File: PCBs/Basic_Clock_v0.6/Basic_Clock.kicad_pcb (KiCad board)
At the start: 2 copper layers, 97.8 x 71.1 mm, 37 parts, among them J1 Conn_01x04_Female, J3 Screw_Terminal_01x02, J4 Screw_Terminal_01x02, J5 Conn_01x03_Female, SW2 SW_Push, SW3 SW_Push, SW4 SW_Push, U1 LM317_TO-220, U2 ATmega328P-PU, U3 MAX485E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

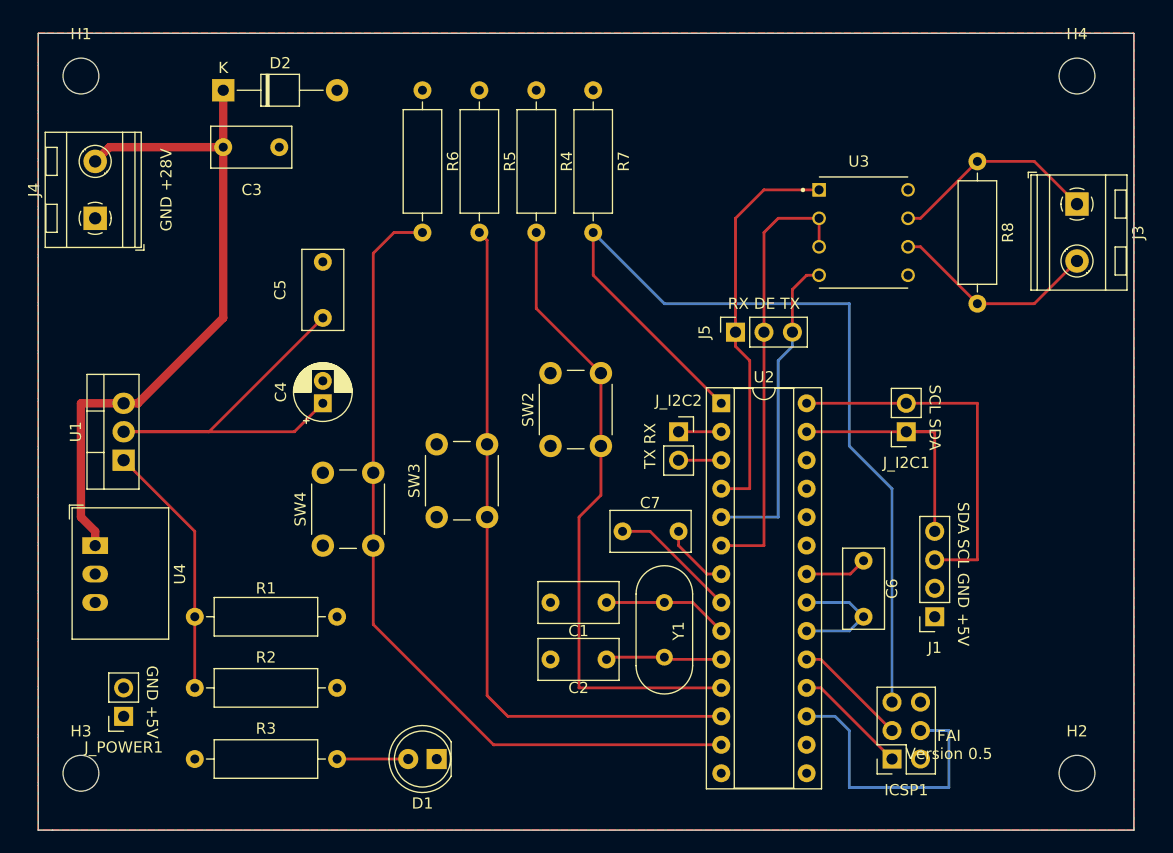
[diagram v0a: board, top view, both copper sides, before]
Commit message: Fixed ICSP Pinout
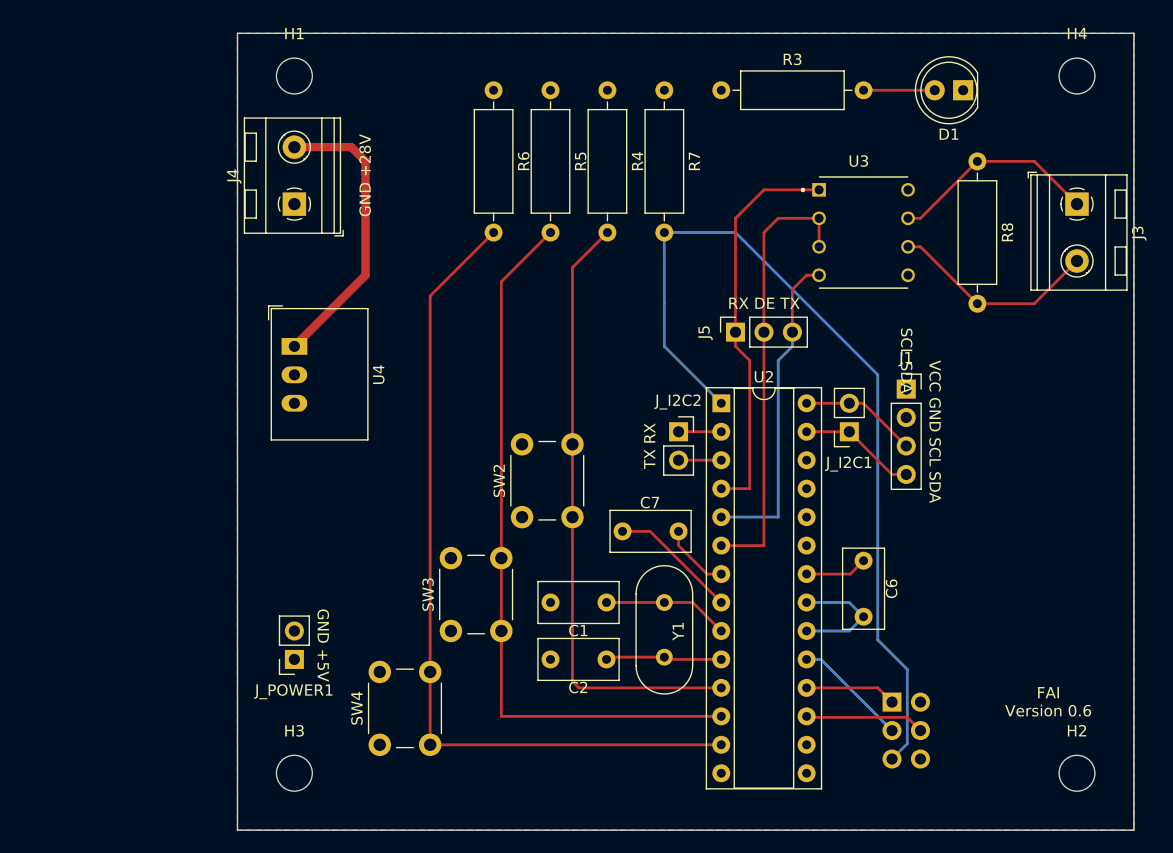
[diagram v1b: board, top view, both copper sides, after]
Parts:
- removed C3, C5: 100nF, Capacitor_THT:C_Rect_L7.0mm_W3.5mm_P5.00mm
- removed C4: 1uF, Capacitor THT:CP_Radial_D5.0mm_P2.00mm
- removed D2: D, Diode THT:D_T-1_P10.16mm_Horizontal
- removed R1: 240, Resistor:R_Axial_DIN0309_L9.0mm_D3.2mm_P12.70mm_Horizontal
- removed R2: 720, Resistor:R_Axial_DIN0309_L9.0mm_D3.2mm_P12.70mm_Horizontal
- removed U1: LM317_TO-220, TO SOT THT:TO-220-3_Vertical
- ICSP1: moved to B.Cu
- moved R3 76.0 mm to (97.8, 109.2)
- moved D1 76.0 mm to (119.4, 109.2)
- moved U4 25.1 mm to (59.7, 132.1)
- moved J1 20.5 mm to (114.3, 135.9), turned to 0 degrees
- moved H1 19.0 mm to (59.7, 108.0)
- moved H3 19.0 mm to (59.7, 170.2)
- moved SW4 18.5 mm to (67.3, 167.6)
- moved J4 17.8 mm to (59.7, 119.4)
- moved J_POWER1 16.1 mm to (59.7, 160.0)
- moved SW3 10.2 mm to (73.7, 157.5)
- moved SW2 6.84 mm to (80.0, 147.3)
- moved R4 6.35 mm to (87.6, 109.2)
- moved R5 6.35 mm to (82.5, 109.2)
- moved R6 6.35 mm to (77.5, 109.2)
- moved R7 6.35 mm to (92.7, 109.2)
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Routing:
- net +5V: track 58.2 -> 17.3 mm
- net +28V: track 61.4 -> 26.0 mm
- net Net-(R1-Pad2): track 23.0 -> 0.00 mm
- net /SCL: track 33.0 -> 10.5 mm
- net /MOSI: track 25.9 -> 10.7 mm
- net /SDA: track 22.9 -> 10.5 mm
- net Net-(ICSP1-Pad5): track 82.6 -> 77.6 mm
- net /MISO: track 10.3 -> 8.15 mm
- net /PIN11: track 56.5 -> 54.9 mm
- net /PIN12: track 63.3 -> 64.6 mm
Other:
- board size 97.8 x 71.1 mm -> 80 x 71.1 mm
- board text added: "FAI Version 0.6"
- board text added: "VCC GND SCL SDA"
- board text removed: "FAI Version 0.5"
- board text removed: "SDA SCL GND +5V"
